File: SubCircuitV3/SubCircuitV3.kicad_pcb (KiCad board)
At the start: 2 copper layers, 121.4 x 121.2 mm, 52 parts, among them J1 JTAG, J10 ESC_POWER, J11 ESC_POWER, J12 ESC_POWER, J13 ESC_POWER, J14 FEMALE XT-60, J15 ESC PWM, J16 5S, J17 Water Sensor Input, J18 3S OUT, J19 2S OUT, J2 ESC PWM, J20 SWITCH, J21 U3V16F15, J22 CAM OUT, J3 ESC PWM, J4 ESC PWM, J5 ESC PWM, J6 ESC PWM, J7 3S, J8 ESC_POWER, J9 ESC_POWER, K1 G5Q-1A, Q1 NMOS, Q2 NMOS, Q3 NMOS, Q4 NMOS, Q5 NMOS, Q6 NMOS

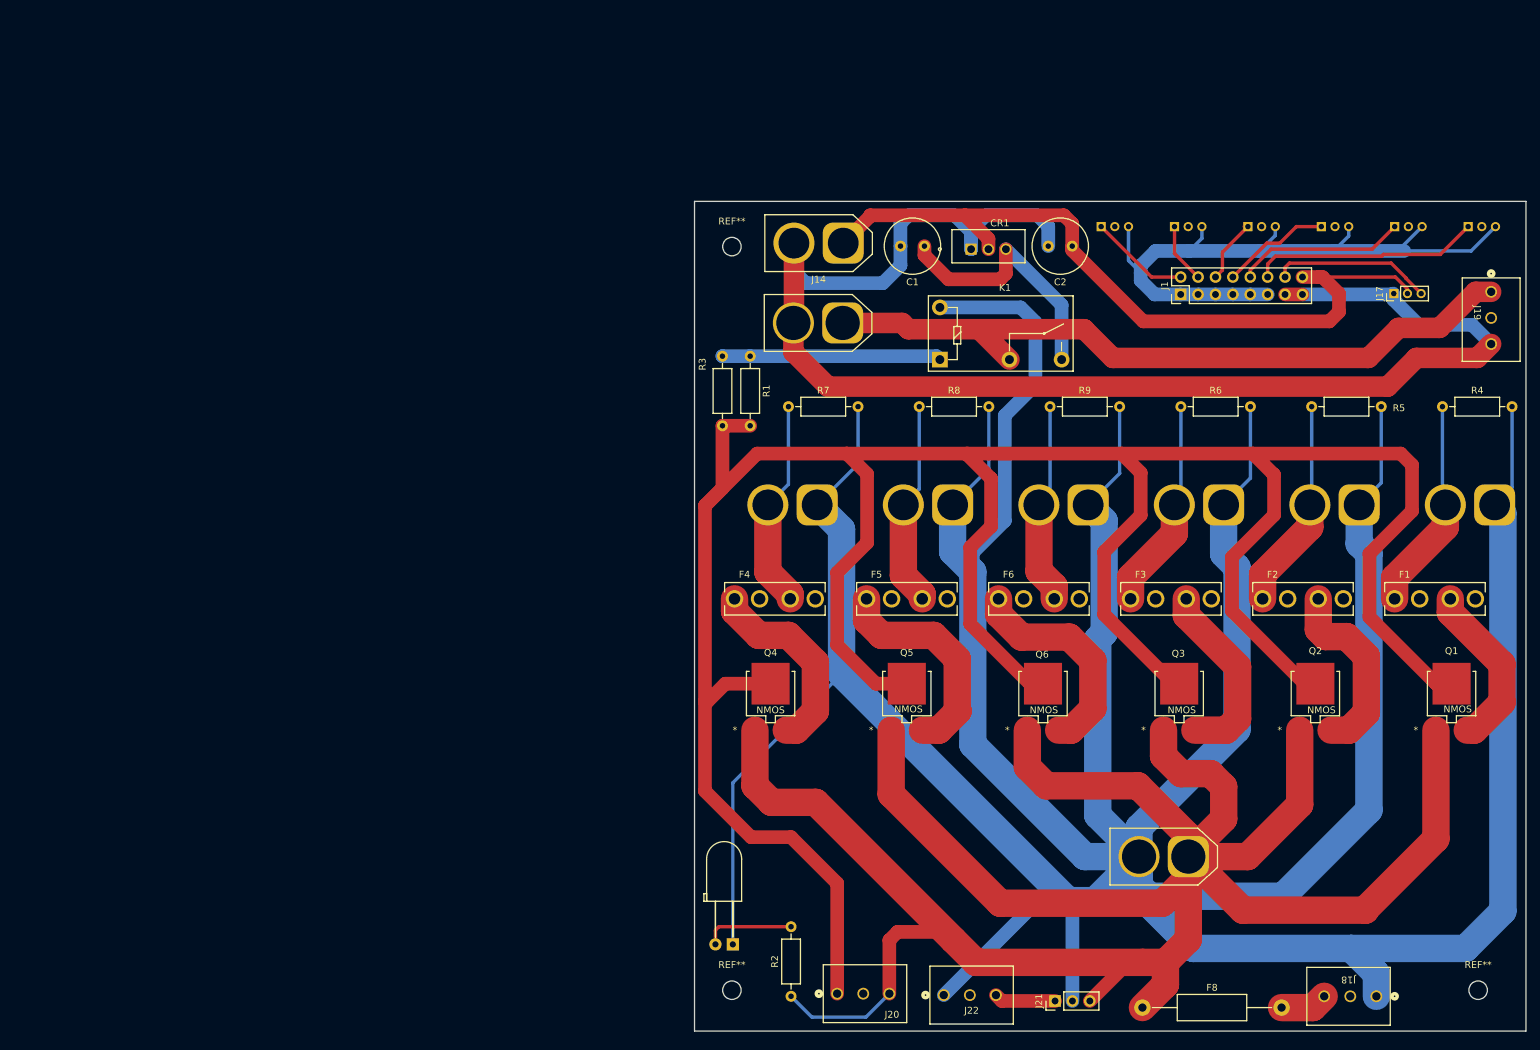
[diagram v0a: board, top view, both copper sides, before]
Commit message: Replaced male with female connectors
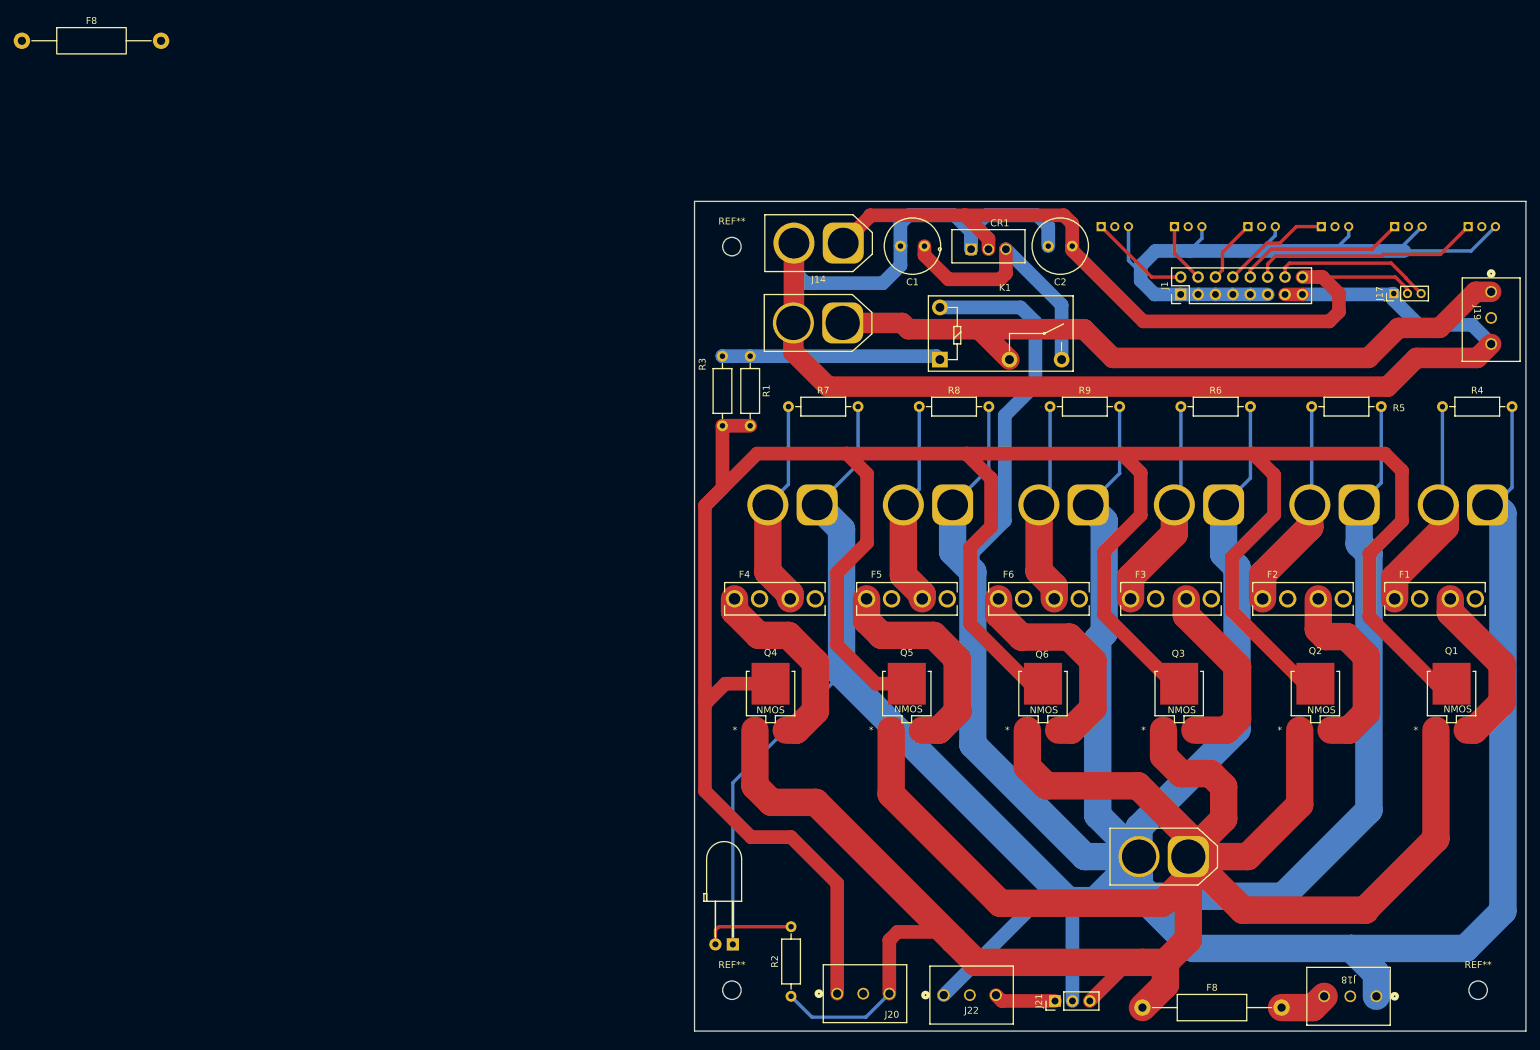
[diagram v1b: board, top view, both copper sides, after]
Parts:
- added F8: Fuse, Resistor_THT:R_Axial_DIN0411_L9.9mm_D3.6mm_P20.32mm_Horizontal, F.Cu at (1.48, 2.08)
- J10, J11, J12, J13, J8, J9: footprint AMASS_XT60-M:AMASS_XT60-M_1x02_P7.20mm_Vertical -> Connector_AMASS:AMASS_XT60-F_1x02_P7.20mm_Vertical
- moved J8 1.03 mm to (215.5, 69.8)
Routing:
- net /SG: track 430.9 -> 428.3 mm
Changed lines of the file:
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@@
 		(embedded_fonts no)
 	)
+	(footprint "Resistor_THT:R_Axial_DIN0411_L9.9mm_D3.6mm_P20.32mm_Horizontal"
+		(layer "F.Cu")
+		(at 1.475 2.075)
+		(descr "Resistor, Axial_DIN0411 series, Axial, Horizontal, pin pitch=20.32mm, 1W, length*diameter=9.9*3.6mm^2")
+		(tags "Resistor Axial_DIN0411 series Axial Horizontal pin pitch 20.32mm 1W length 9.9mm diameter 3.6mm")
+		(property "Reference" "F8"
+			(at 10.16 -2.92 0)
+			(layer "F.SilkS")
+			(effects
+				(font
+					(size 1 1)
+					(thickness 0.15)
+				)
+			)
+		)
+		(property "Value" "Fuse"
+			(at 10.16 2.92 0)
+			(layer "F.Fab")
+			(effects
+				(font
+					(size 1 1)
+					(thickness 0.15)
+				)
+			)
+		)
+		(property "Datasheet" "~"
+			(at 0 0 0)
+			(layer "F.Fab")
+			(hide yes)
+			(effects
+				(font
+					(size 1.27 1.27)
+					(thickness 0.15)
+				)
+			)
+		)
+		(property "Description" "Fuse"
+			(at 0 0 0)
+			(layer "F.Fab")
+			(hide yes)
+			(effects
+				(font
+					(size 1.27 1.27)
+					(thickness 0.15)
+				)
+			)
+		)
+		(property ki_fp_filters "*Fuse*")
+		(sheetname "/")
+		(sheetfile "SubCircuitV3.kicad_sch")
+		(attr through_hole)
+		(fp_line
+			(start 1.44 0)
+			(end 5.09 0)
+			(stroke
+				(width 0.12)
+				(type solid)
+			)
+			(layer "F.SilkS")
+		)
+		(fp_line
+			(start 18.88 0)
+			(end 15.23 0)
+			(stroke
+				(width 0.12)
+				(type solid)
+			)
+			(layer "F.SilkS")
+		)
+		(fp_rect
+			(start 5.09 -1.92)
+			(end 15.23 1.92)
+			(stroke
+				(width 0.12)
+				(type solid)
+			)
+			(fill no)
+			(layer "F.SilkS")
+		)
+		(fp_rect
+			(start -1.45 -2.05)
+			(end 21.77 2.05)
+			(stroke
+				(width 0.05)
+				(type solid)
+			)
+			(fill no)
+			(layer "F.CrtYd")
+		)
+		(fp_line
+			(start 0 0)
+			(end 5.21 0)
+			(stroke
+				(width 0.1)
+				(type solid)
+			)
+			(layer "F.Fab")
+		)
+		(fp_line
+			(start 20.32 0)
+			(end 15.11 0)
+			(stroke
+				(width 0.1)
+				(type solid)
+			)
+			(layer "F.Fab")
+		)
+		(fp_rect
+			(start 5.21 -1.8)
+			(end 15.11 1.8)
+			(stroke
+				(width 0.1)
+				(type solid)
+			)
+			(fill no)
+			(layer "F.Fab")
+		)
+		(fp_text user "${REFERENCE}"
+			(at 10.16 0 0)
+			(layer "F.Fab")
+			(effects
+				(font
+					(size 1 1)
+					(thickness 0.15)
+				)
+			)
+		)
+		(pad "1" thru_hole circle
+			(at 0 0)
+			(size 2.4 2.4)
+			(drill 1.2)
+			(layers "*.Cu" "*.Mask")
+			(remove_unused_layers no)
+			(net 14 "+12V")
+			(pintype "passive")
+		)
+		(pad "2" thru_hole circle
+			(at 20.32 0)
+			(size 2.4 2.4)
+			(drill 1.2)
+			(layers "*.Cu" "*.Mask")
+			(remove_unused_layers no)
+			(net 39 "Net-(J18-Pin_3)")
+			(pintype "passive")
+		)
+		(embedded_fonts no)
+		(model "${KICAD9_3DMODEL_DIR}/Resistor_THT.3dshapes/R_Axial_DIN0411_L9.9mm_D3.6mm_P20.32mm_Horizontal.step"
+			(offset
+				(xyz 0 0 0)
+			)
+			(scale
+				(xyz 1 1 1)
+			)
+			(rotate
+				(xyz 0 0 0)
+			)
+		)
+	)
 	(footprint "284932-3:CONN3_284392-3_TEC"
 		(layer "F.Cu")
@@
 		)
 	)
-	(footprint "AMASS_XT60-M:AMASS_XT60-M_1x02_P7.20mm_Vertical"
+	(footprint "Connector_AMASS:AMASS_XT60-F_1x02_P7.20mm_Vertical"
 		(layer "B.Cu")
-		(at 216.535 69.85 180)
+		(at 215.5 69.85 180)
 		(descr "AMASS female XT60, through hole, vertical, https://www.tme.eu/Document/2d152ced3b7a446066e6c419d84bb460/XT60%20SPEC.pdf")
 		(tags "XT60 female vertical")
@@
 		(property "Datasheet" "~"
 			(at 0 0 0)
+			(unlocked yes)
 			(layer "B.Fab")
 			(hide yes)
@@
 		(property "Description" ""
 			(at 0 0 0)
+			(unlocked yes)
 			(layer "B.Fab")
 			(hide yes)
@@
 		)
 		(embedded_fonts no)
-		(model "${KISYS3DMOD}/Connector_AMASS.3dshapes/AMASS_XT60-M_1x02_P7.2mm_Vertical.wrl"
+		(model "${KICAD9_3DMODEL_DIR}/Connector_AMASS.3dshapes/AMASS_XT60-F_1x02_P7.2mm_Vertical.step"
 			(offset
 				(xyz 0 0 0)
@@
 		)
 	)
-	(footprint "AMASS_XT60-M:AMASS_XT60-M_1x02_P7.20mm_Vertical"
+	(footprint "Connector_AMASS:AMASS_XT60-F_1x02_P7.20mm_Vertical"
 		(layer "B.Cu")
 		(at 117.602 69.85 180)
@@
 		(property "Datasheet" "~"
 			(at 0 0 0)
+			(unlocked yes)
 			(layer "B.Fab")
 			(hide yes)
@@
 		(property "Description" ""
 			(at 0 0 0)
+			(unlocked yes)
 			(layer "B.Fab")
 			(hide yes)
@@
 		)
 		(embedded_fonts no)
-		(model "${KISYS3DMOD}/Connector_AMASS.3dshapes/AMASS_XT60-M_1x02_P7.2mm_Vertical.wrl"
+		(model "${KICAD9_3DMODEL_DIR}/Connector_AMASS.3dshapes/AMASS_XT60-F_1x02_P7.2mm_Vertical.step"
 			(offset
 				(xyz 0 0 0)
@@
 		)
 	)
-	(footprint "AMASS_XT60-M:AMASS_XT60-M_1x02_P7.20mm_Vertical"
+	(footprint "Connector_AMASS:AMASS_XT60-F_1x02_P7.20mm_Vertical"
 		(layer "B.Cu")
 		(at 137.3886 69.85 180)
@@
 		(property "Datasheet" "~"
 			(at 0 0 0)
+			(unlocked yes)
 			(layer "B.Fab")
 			(hide yes)
@@
 		(property "Description" ""
 			(at 0 0 0)
+			(unlocked yes)
 			(layer "B.Fab")
 			(hide yes)
@@
 		)
 		(embedded_fonts no)
-		(model "${KISYS3DMOD}/Connector_AMASS.3dshapes/AMASS_XT60-M_1x02_P7.2mm_Vertical.wrl"
+		(model "${KICAD9_3DMODEL_DIR}/Connector_AMASS.3dshapes/AMASS_XT60-F_1x02_P7.2mm_Vertical.step"
 			(offset
 				(xyz 0 0 0)
@@
 		)
 	)
-	(footprint "AMASS_XT60-M:AMASS_XT60-M_1x02_P7.20mm_Vertical"
+	(footprint "Connector_AMASS:AMASS_XT60-F_1x02_P7.20mm_Vertical"
 		(layer "B.Cu")
 		(at 157.1752 69.85 180)
@@
 		(property "Datasheet" "~"
 			(at 0 0 0)
+			(unlocked yes)
 			(layer "B.Fab")
 			(hide yes)
@@
 		(property "Description" ""
 			(at 0 0 0)
+			(unlocked yes)
 			(layer "B.Fab")
 			(hide yes)
@@
 		)
 		(embedded_fonts no)
-		(model "${KISYS3DMOD}/Connector_AMASS.3dshapes/AMASS_XT60-M_1x02_P7.2mm_Vertical.wrl"
+		(model "${KICAD9_3DMODEL_DIR}/Connector_AMASS.3dshapes/AMASS_XT60-F_1x02_P7.2mm_Vertical.step"
 			(offset
 				(xyz 0 0 0)
@@
 		)
 	)
-	(footprint "AMASS_XT60-M:AMASS_XT60-M_1x02_P7.20mm_Vertical"
+	(footprint "Connector_AMASS:AMASS_XT60-F_1x02_P7.20mm_Vertical"
 		(layer "B.Cu")
 		(at 176.9618 69.85 180)
@@
 			(at 3.6 -5.4 0)
 			(layer "B.Fab")
-			(hide yes)
 			(effects
 				(font
@@
 		(property "Datasheet" "~"
 			(at 0 0 0)
+			(unlocked yes)
 			(layer "B.Fab")
 			(hide yes)
@@
 		(property "Description" ""
 			(at 0 0 0)
+			(unlocked yes)
 			(layer "B.Fab")
 			(hide yes)
@@
 		)
 		(embedded_fonts no)
-		(model "${KISYS3DMOD}/Connector_AMASS.3dshapes/AMASS_XT60-M_1x02_P7.2mm_Vertical.wrl"
+		(model "${KICAD9_3DMODEL_DIR}/Connector_AMASS.3dshapes/AMASS_XT60-F_1x02_P7.2mm_Vertical.step"
 			(offset
 				(xyz 0 0 0)
@@
 		)
 	)
-	(footprint "AMASS_XT60-M:AMASS_XT60-M_1x02_P7.20mm_Vertical"
+	(footprint "Connector_AMASS:AMASS_XT60-F_1x02_P7.20mm_Vertical"
 		(layer "B.Cu")
 		(at 196.7484 69.85 180)
@@
 		(property "Datasheet" "~"
 			(at 0 0 0)
+			(unlocked yes)
 			(layer "B.Fab")
 			(hide yes)
@@
 		(property "Description" ""
 			(at 0 0 0)
+			(unlocked yes)
 			(layer "B.Fab")
 			(hide yes)
@@
 		)
 		(embedded_fonts no)
-		(model "${KISYS3DMOD}/Connector_AMASS.3dshapes/AMASS_XT60-M_1x02_P7.2mm_Vertical.wrl"
+		(model "${KICAD9_3DMODEL_DIR}/Connector_AMASS.3dshapes/AMASS_XT60-F_1x02_P7.2mm_Vertical.step"
 			(offset
 				(xyz 0 0 0)
@@
 	)
 	(segment
+		(start 207.9752 95.9612)
+		(end 198.247 86.233)
+		(width 2)
+		(layer "F.Cu")
+		(net 22)
+	)
+	(segment
+		(start 210.2443 95.9612)
+		(end 207.9752 95.9612)
+		(width 2)
+		(layer "F.Cu")
+		(net 22)
+	)
+	(segment
 		(start 101.219 98.552)
 		(end 101.219 111.633)
@@
 	)
 	(segment
-		(start 101.219 69.977)
-		(end 103.773 67.423)
+		(start 203 64.857)
+		(end 200.5 62.357)
 		(width 2)
 		(layer "F.Cu")
@@
 	)
 	(segment
-		(start 184.186 65.314)
-		(end 184.3255 65.4535)
+		(start 101.219 69.977)
+		(end 103.773 67.423)
 		(width 2)
 		(layer "F.Cu")
@@
 	)
 	(segment
-		(start 204.47 70.739)
-		(end 198.247 76.962)
+		(start 184.186 65.314)
+		(end 184.3255 65.4535)
 		(width 2)
 		(layer "F.Cu")
@@
 	)
 	(segment
-		(start 198.247 76.962)
-		(end 198.247 86.233)
-		(width 2)
-		(layer "F.Cu")
-		(net 22)
-	)
-	(segment
 		(start 101.219 98.552)
 		(end 101.6 98.552)
@@
 	)
 	(segment
+		(start 203 72.209)
+		(end 203 64.857)
+		(width 2)
+		(layer "F.Cu")
+		(net 22)
+	)
+	(segment
+		(start 198.247 86.233)
+		(end 198.247 76.962)
+		(width 2)
+		(layer "F.Cu")
+		(net 22)
+	)
+	(segment
 		(start 120.523 79.756)
 		(end 120.523 90.297)
@@
 	)
 	(segment
-		(start 210.2443 95.9612)
-		(end 207.9752 95.9612)
+		(start 159.512 76.708)
+		(end 159.512 85.852)
 		(width 2)
 		(layer "F.Cu")
@@
 	)
 	(segment
-		(start 159.512 76.708)
-		(end 159.512 85.852)
+		(start 198.247 76.962)
+		(end 203 72.209)
 		(width 2)
 		(layer "F.Cu")
@@
 	)
 	(segment
-		(start 207.9752 95.9612)
-		(end 198.247 86.233)
-		(width 2)
-		(layer "F.Cu")
-		(net 22)
-	)
-	(segment
 		(start 139.5 62.357)
 		(end 121.92 62.357)
@@
 	)
 	(segment
-		(start 202.819 62.357)
-		(end 204.47 64.008)
-		(width 2)
-		(layer "F.Cu")
-		(net 22)
-	)
-	(segment
 		(start 181.229 62.357)
-		(end 202.819 62.357)
+		(end 200.5 62.357)
 		(width 2)
 		(layer "F.Cu")
@@
 		(width 2)
 		(layer "F.Cu")
-		(net 22)
-	)
-	(segment
-		(start 204.47 64.008)
-		(end 204.47 70.739)
-		(width 2)
-		(layer "F.Cu")

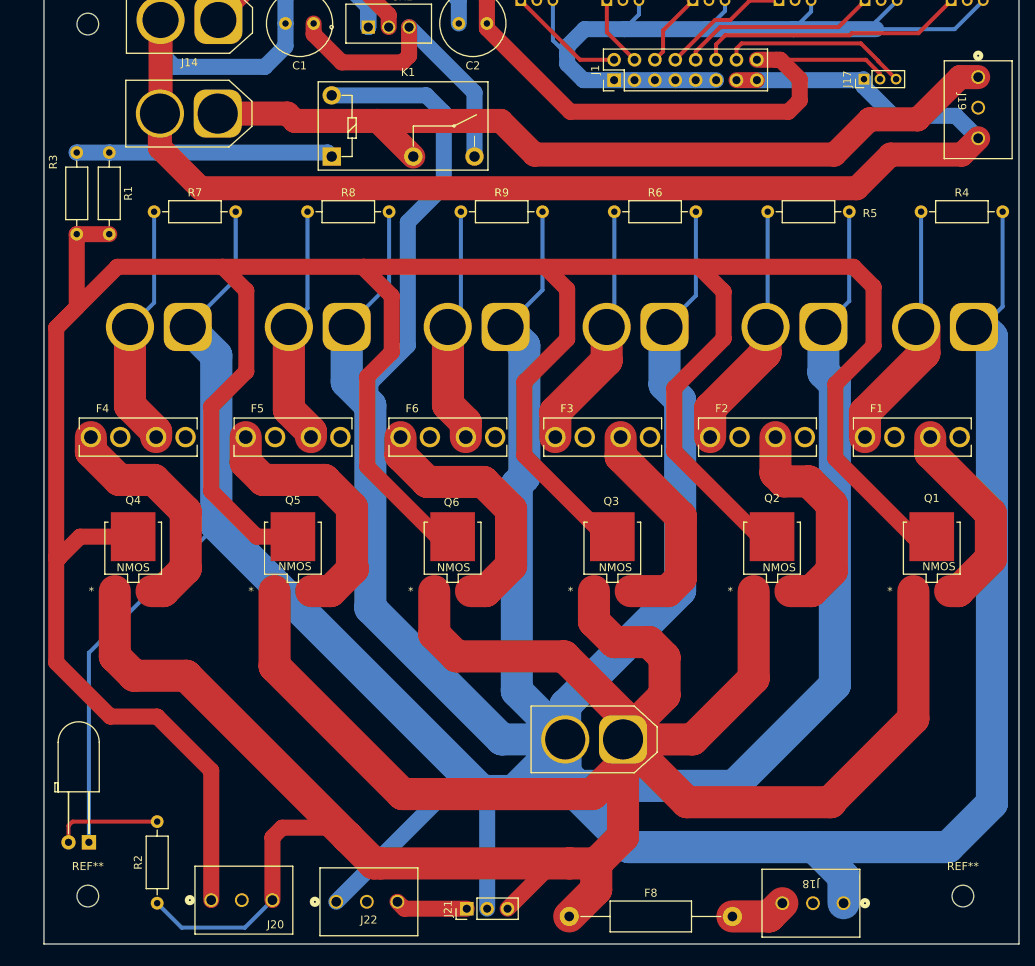
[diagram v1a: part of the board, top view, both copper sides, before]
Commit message: Rearranged PCB layout to make room for boost convertor
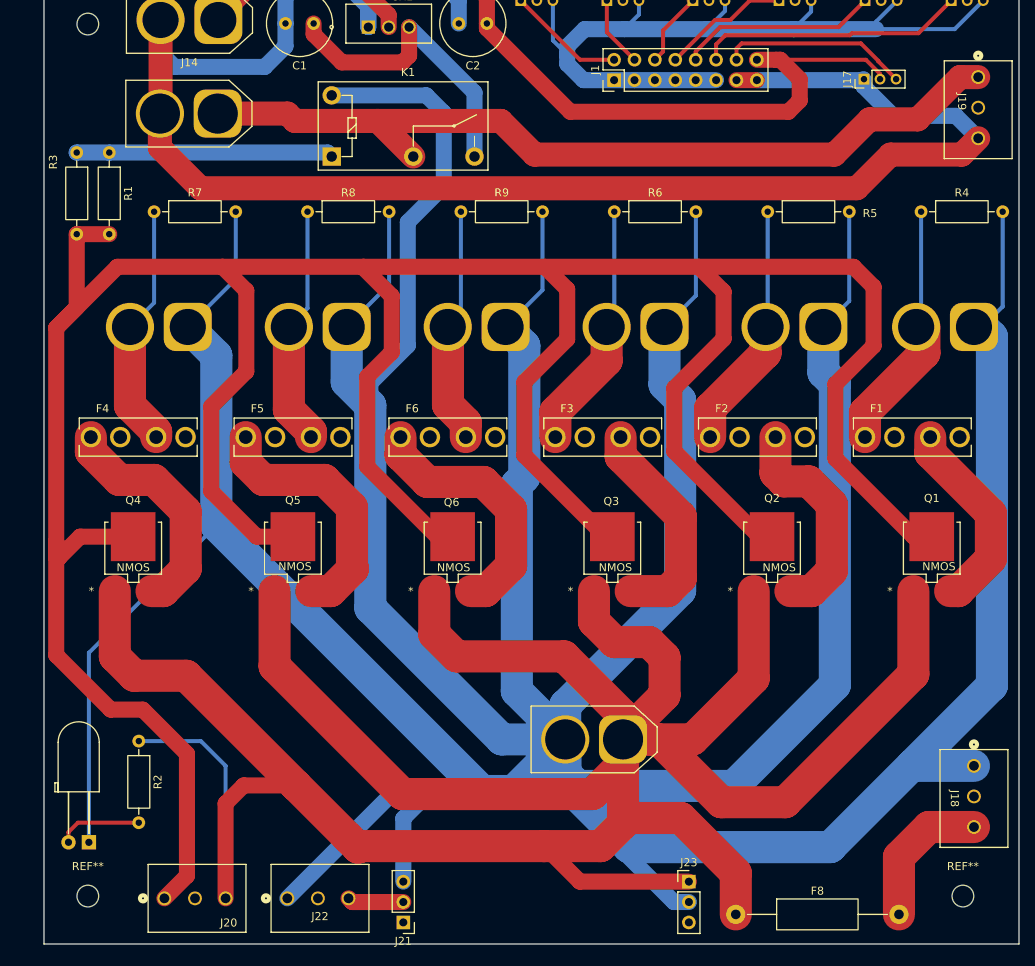
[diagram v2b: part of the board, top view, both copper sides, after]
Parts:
- added J23: U3V16F15, Connector_PinHeader_2.54mm:PinHeader_1x03_P2.54mm_Vertical, F.Cu at (180.0, 138.9)
- moved J18 23.6 mm to (215.5, 124.5), turned to -90 degrees
- moved F8 20.7 mm to (185.8, 143.0)
- moved R2 20.3 mm to (111.5, 121.4), turned to -90 degrees
- moved J21 8.08 mm to (144.4, 144.0), turned to 180 degrees
- moved J22 6.11 mm to (130.0, 141.0)
- moved J20 5.84 mm to (114.7, 141.0)
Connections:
- J21 pad 1: Net-(J21-Pin_1) -> unconnected-(J21-Pin_1-Pad1)
- J21 pad 2: GND1 -> Net-(J21-Pin_2)
- J21 pad 3: +12V -> GND1
- J22 pad 3: Net-(J21-Pin_1) -> Net-(J21-Pin_2)
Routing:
- net +12V: track 365.5 -> 400.0 mm
- net Net-(J18-Pin_3): track 6.91 -> 18.0 mm
- net GND1: track 724.5 -> 734.1 mm
- net Net-(J21-Pin_1): track 8.99 -> 0.00 mm
- net Net-(J21-Pin_2): track 0.00 -> 7.01 mm
- net Net-(D1-A): track 13.3 -> 10.5 mm
- net /SG: track 428.3 -> 429.0 mm
